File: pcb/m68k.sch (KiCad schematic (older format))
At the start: 14 parts

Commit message: add rtdi sd and ps2
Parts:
- removed U?: IS61C5128AL-10KLI, Package_SO:SOJ-36_10.16x23.49mm_P1.27mm, symbol Memory_RAM:IS61C5128AL-10KLI
- added C?: CP1, symbol Device:CP1
- added C?: 0.1uF, symbol Device:C
- added J?: AudioJack2, symbol Connector:AudioJack2
- added J?: SD_Card, symbol Connector:SD_Card
- added J?: DB15_Male_HighDensity, symbol Connector:DB15_Male_HighDensity
- added J?: USB_B_Micro, symbol Connector:USB_B_Micro
- added J?: Mini-DIN-6, symbol Connector:Mini-DIN-6
- added R? (x2): 120, symbol Device:R
- added R? (x2): 2, symbol Device:R
- added U?: FT232RL, Package_SO:SSOP-28_5.3x10.2mm_P0.65mm, symbol Interface_USB:FT232RL
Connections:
- net labels added: +3.3V, +5V, GND
- wire segments 185 -> 251
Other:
- note removed: "SRAM\n"

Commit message: Cleanup schematic and fix errors
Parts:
- C?: symbol Device:CP1 -> m68k-rescue:CP1-Device
- C?: symbol Device:C -> m68k-rescue:C-Device
- J?: symbol Connector:AudioJack2 -> m68k-rescue:AudioJack2-Connector
- J?: symbol Connector:SD_Card -> m68k-rescue:SD_Card-Connector
- J?: symbol Connector:DB15_Male_HighDensity -> m68k-rescue:DB15_Male_HighDensity-Connector
- J?: symbol Connector:USB_B_Micro -> m68k-rescue:USB_B_Micro-Connector
- J?: symbol Connector:Mini-DIN-6 -> m68k-rescue:Mini-DIN-6-Connector
- R? (x4): symbol Device:R -> m68k-rescue:R-Device
- U?: symbol CPU_NXP_68000:68000D -> m68k-rescue:68000D-CPU_NXP_68000
- U? (x6): symbol Lattice_iCE_FPGA:iCE40-HX4K-TQ144 -> m68k-rescue:iCE40-HX4K-TQ144-Lattice_iCE_FPGA
- U?: symbol Interface_USB:FT232RL -> m68k-rescue:FT232RL-Interface_USB
- U? (x3): symbol Logic_LevelTranslator:TXB0108DQSR -> m68k-rescue:TXB0108DQSR-Logic_LevelTranslator
- U?: symbol Memory_RAM:AS6C1616 -> m68k-rescue:AS6C1616-Memory_RAM
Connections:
- net labels added: a1, a10, a11, a12, a13, a14, a15, a16, a17, a18, a19, a2, a20, a21, a22, a23, a24, a3, a4, a5, a6, a7, a8, a9, d0, d1, d10, d11, d12, d13, d14, d15, d2, d3, d4, d5, d6, d7, d8, d9
- net labels removed: A24, A25, Unnecessary?
- wire segments 251 -> 265
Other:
- note removed: "Could be hooked up directly\n"
- moved on the sheet: U?

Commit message: add vga dac and start control pins
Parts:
- removed R? (x2): 120, symbol m68k-rescue:R-Device
- added C?: 0.1uF, symbol Device:C
- added R?: R, symbol Device:R
- added U?: ADV7125KSTZ50, ST_48, symbol 2019-05-17_15-12-34:ADV7125KSTZ50
- added U? (x2): TXB0108DQSR, Package_SON:USON-20_2x4mm_P0.4mm, symbol m68k-rescue:TXB0108DQSR-Logic_LevelTranslator-m68k-rescue
- C?: symbol m68k-rescue:CP1-Device -> m68k-rescue:CP1-Device-m68k-rescue
- C?: symbol m68k-rescue:C-Device -> m68k-rescue:C-Device-m68k-rescue
- J?: symbol m68k-rescue:AudioJack2-Connector -> m68k-rescue:AudioJack2-Connector-m68k-rescue
- J?: symbol m68k-rescue:SD_Card-Connector -> m68k-rescue:SD_Card-Connector-m68k-rescue
- J?: symbol m68k-rescue:DB15_Male_HighDensity-Connector -> m68k-rescue:DB15_Male_HighDensity-Connector-m68k-rescue
- J?: symbol m68k-rescue:USB_B_Micro-Connector -> m68k-rescue:USB_B_Micro-Connector-m68k-rescue
- J?: symbol m68k-rescue:Mini-DIN-6-Connector -> m68k-rescue:Mini-DIN-6-Connector-m68k-rescue
- R? (x2): symbol m68k-rescue:R-Device -> m68k-rescue:R-Device-m68k-rescue
- U?: symbol m68k-rescue:68000D-CPU_NXP_68000 -> m68k-rescue:68000D-CPU_NXP_68000-m68k-rescue
- U?: symbol m68k-rescue:FT232RL-Interface_USB -> m68k-rescue:FT232RL-Interface_USB-m68k-rescue
- U? (x3): symbol m68k-rescue:TXB0108DQSR-Logic_LevelTranslator -> m68k-rescue:TXB0108DQSR-Logic_LevelTranslator-m68k-rescue
- U?: symbol m68k-rescue:AS6C1616-Memory_RAM -> m68k-rescue:AS6C1616-Memory_RAM-m68k-rescue
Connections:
- net labels added: R0, R1, R2, R3, R4, R5, R6, R7, hsync, vsync
- wire segments 265 -> 437
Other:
- moved on the sheet: R?, U?A, U?C, U?D, U?F

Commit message: Clean-up some signals
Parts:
- added U?: TXB0108DQSR, Package_SON:USON-20_2x4mm_P0.4mm, symbol m68k-rescue:TXB0108DQSR-Logic_LevelTranslator-m68k-rescue
- C?: symbol Device:C -> m68k-rescue:C-Device
- R?: symbol Device:R -> m68k-rescue:R-Device
- U?: symbol 2019-05-17_15-12-34:ADV7125KSTZ50 -> m68k-rescue:ADV7125KSTZ50-2019-05-17_15-12-34
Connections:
- net labels added: ASn, BERRn, BGACKn, BGn, BRn, CLK, DTACKn, E, FC0, FC1, FC2, HALTn, IPL0n, IPL1n, IPL2n, LDSn, RESETn, R_Wn, UDSn, VMAn, VPAn
- wire segments 437 -> 464
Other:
- note added: "Not level converted,\nbut it’ll be fine\n(probably)"
- moved on the sheet: U?, U?A, U?B, U?E, U?F

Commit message: Fix mostly everything
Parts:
- removed C?: CP1, symbol m68k-rescue:CP1-Device-m68k-rescue
- removed C?: 0.1uF, symbol m68k-rescue:C-Device-m68k-rescue
- removed C?: 0.1uF, symbol m68k-rescue:C-Device
- removed J?: AudioJack2, symbol m68k-rescue:AudioJack2-Connector-m68k-rescue
- removed R? (x2): 2, symbol m68k-rescue:R-Device-m68k-rescue
- removed R?: R, symbol m68k-rescue:R-Device
- removed U?: FT232RL, Package_SO:SSOP-28_5.3x10.2mm_P0.65mm, symbol m68k-rescue:FT232RL-Interface_USB-m68k-rescue
- removed U?: TXB0108DQSR, Package_SON:USON-20_2x4mm_P0.4mm, symbol m68k-rescue:TXB0108DQSR-Logic_LevelTranslator-m68k-rescue
- added C1, C10, C11, C12, C13, C14, C15, C16, C17, C18, C19, C2, C21, C22, C4, C6, C7: 0.1uF, symbol Device:C
- added C20: 0.1uF, symbol Device:C_Small
- added C3, C9: 10uF, symbol Device:C
- added C5, C8: 4.7uF, symbol Device:C
- added D1: D_Schottky, symbol Device:D_Schottky
- added D2: AD1580, symbol Device:D
- added R1, R10, R11, R12, R13, R14, R15, R2, R3, R4, R8: 10k, symbol Device:R
- added R16: 1k, symbol Device:R
- added R17, R18, R19: 75, symbol Device:R
- added R20: 530, symbol Device:R_Small
- added R5, R6, R7: 2.2k, symbol Device:R
- added R9: 100, symbol Device:R
- added U1: 93LC56, symbol Memory_EEPROM:93LCxxC
- added U10: 25LCxxx, symbol Memory_EEPROM:25LCxxx
- added U3: FT2232H, symbol Interface_USB:FT2232H
- added X1: ASV-12.000MHz, Oscillator:Oscillator_SMD_Abracon_ASV-4Pin_7.0x5.1mm, symbol Oscillator:ASV-xxxMHz
- gave numbers to parts that had none: 15
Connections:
- net hsync is gone; now on net HSYNC: J4.13
- net vsync is gone; now on net VSYNC: J4.14
- net +3V3: now also J1.1 (VBUS), J3.4 (VDD), U11.5 (VCCA), U11.6 (OE), U12.5 (VCCA), U12.6 (OE), U13.100 (VCCIO_1[2]), U13.123 (VCCIO_0[2]), U13.131 (VCCIO_0[2]), U13.30 (VCCIO_3[2]), U13.46 (VCCIO_2[2]), U13.57 (VCCIO_2[2]), U13.6 (VCCIO_3[2]), U13.72 (VCC_SPI), U13.89 (VCCIO_1[2]), U14.13 (VAA), U14.29 (VAA), U14.30 (VAA), U14.38 (PSAVE*), U4.5 (VCCA), U4.6 (OE), U5.5 (VCCA), U5.6 (OE), U6.5 (VCCA), U6.6 (OE), U7.1 (VCCA), U8.1 (VCCA), U9.37 (VCC), C1.1, C11.1, C12.1, C13.1, C14.1, C15.1, C16.1, C17.1, C19.1, C2.1, C20.2, C21.1, C22.1, C5.1, C6.1, C7.1, C8.1, D1.2 (A), R10.2, R11.2, R12.2, R15.2, R16.2, R2.2, R3.2, R4.2, R6.2, R8.2, U1.6 (ORG), U1.8 (VCC), U10.8 (VCC), U3.20 (VCCIO), U3.31 (VCCIO), U3.4 (VPHY), U3.42 (VCCIO), U3.50 (VREGIN), U3.56 (VCCIO), U3.9 (VPLL), X1.1 (EN), X1.4 (Vdd); no longer J3.3 (VSS), J3.6 (VSS)
- net +5V: now also J4.9, U11.19 (VCCB), U12.19 (VCCB), U2.14 (VCC), U2.49 (VCC), U4.19 (VCCB), U5.19 (VCCB), U6.19 (VCCB), U7.23 (VCCB), U7.24 (VCCB), U8.23 (VCCB), U8.24 (VCCB), R13.1, R14.1; no longer U14.29 (VAA), U14.30 (VAA)
- net ASn: now also U11.16 (B4); no longer U11.17 (B3)
- net BGACKn: now also U13.42 (IOB_64); no longer U12.20 (B1)
- net BGn: now also U11.15 (B5); no longer U12.18 (B2)
- net BRn: now also U13.43 (IOB_71); no longer U12.17 (B3)
- net DTACKn: now also U13.37 (IOB_56); no longer U11.15 (B5)
- net E: now also U11.13 (B7); no longer U12.15 (B5)
- net FC0: now also U12.20 (B1)
- net FC1: now also U12.18 (B2)
- net FC2: now also U12.17 (B3)
- net GND: now also J3.3 (VSS), J3.6 (VSS), J4.10, J4.5, U13.103 (GND[9]), U13.13 (GND[9]), U13.132 (GND[9]), U13.14 (GND[9]), U13.140 (GND[9]), U13.5 (GND[9]), U13.59 (GND[9]), U13.69 (GND[9]), U13.86 (GND[9]), U14.12 (SYNC*), C1.2, C11.2, C12.2, C13.2, C14.2, C15.2, C16.2, C17.2, C18.2, C19.2, C2.2, C21.2, C22.2, C3.2, C4.2, C5.2, C6.2, C7.2, C8.2, D2.2 (A), R1.2, R17.2, R18.2, R19.2, R20.2, R5.2, U1.5 (GND), U10.4 (GND), U3.1 (GND), U3.10 (AGND), U3.11 (GND), U3.13 (TEST), U3.15 (GND), U3.25 (GND), U3.35 (GND), U3.47 (GND), U3.5 (GND), U3.51 (GND), X1.2 (GND); no longer J3.4 (VDD), J4.6, J4.7, J4.8
- net HALTn: now also U11.12 (B8)
- net IPL0n: now also U13.38 (IOB_57); no longer U11.14 (B6)
- net IPL1n: now also U13.39 (IOB_61); no longer U11.13 (B7)
- net IPL2n: now also U13.41 (IOB_63); no longer U11.12 (B8)
- net LDSn: now also U11.17 (B3); no longer U11.18 (B2)
- net RESETn: now also U12.16 (B4), R1.1
- net R_Wn: now also U11.20 (B1); no longer U11.16 (B4)
- net UDSn: now also U11.18 (B2); no longer U11.20 (B1)
- net VMAn: now also U11.14 (B6); no longer U12.16 (B4)
- net VPAn: now also U13.44 (IOB_72); no longer U12.14 (B6)
- net a1: now also U13.134 (IOT_212); no longer U13.130 (IOT_206)
- net a10: now also U13.119 (IOT_178); no longer U13.118 (IOT_177)
- net a11: now also U13.118 (IOT_177); no longer U13.117 (IOT_174)
- net a12: now also U13.117 (IOT_174); no longer U13.116 (IOT_173)
- net a13: now also U13.116 (IOT_173); no longer U13.115 (IOT_172)
- net a14: now also U13.115 (IOT_172); no longer U13.114 (IOT_171)
- net a15: now also U13.114 (IOT_171); no longer U13.113 (IOT_170)
- net a16: now also U13.113 (IOT_170); no longer U13.112 (IOT_169)
- net a17: now also U13.112 (IOT_169); no longer U13.110 (IOT_168)
- net a18: now also U13.110 (IOT_168); no longer U13.30 (VCCIO_3[2]), U13.6 (VCCIO_3[2])
- net a2: now also U13.130 (IOT_206); no longer U13.129 (IOT_198_GBIN0)
- net a3: now also U13.129 (IOT_198_GBIN0); no longer U13.128 (IOT_197_GBIN1)
- net a4: now also U13.128 (IOT_197_GBIN1); no longer U13.125 (IOT_192)
- net a5: now also U13.125 (IOT_192); no longer U13.124 (IOT_191)
- net a6: now also U13.124 (IOT_191); no longer U13.122 (IOT_190)
- net a7: now also U13.122 (IOT_190); no longer U13.121 (IOT_181)
- net a8: now also U13.121 (IOT_181); no longer U13.120 (IOT_179)
- net a9: now also U13.120 (IOT_179); no longer U13.119 (IOT_178)
- net at U11.3 (A3): now also U13.28 (IOL_23A), U9.15 (LB#); no longer U13.134 (IOT_212)
- net at U13.144 (IOT_222): no longer U12.4 (A4)
- net at U13.108 (VPP_2V5): now also D1.1 (K)
- net +1V2: now reaches U13.111 (VCC[4]), U13.27 (VCC[4]), U13.40 (VCC[4]), U13.92 (VCC[4])
- net +1V2: now also R9.2
- net at U13.126 (VCCPLL1): now also U13.54 (VCCPLL0), C10.1, C9.1, R9.1
- net at U13.127 (GNDPLL1): now also U13.53 (GNDPLL0), C10.2, C9.2
- net b6: now reaches U14.22 (B6)
- net b6: now also U13.99 (IOR_152); no longer U13.101 (IOR_160)
- net at U13.102 (IOR_161): now also U14.11 (BLANK*); no longer U14.23 (B7)
- net HSYNC: now reaches U13.105 (IOR_165)
- net VSYNC: now reaches U13.106 (IOR_166)
- net DIR: now reaches U13.107 (IOR_167)
- net DIR: now also U7.2 (DIR), U8.2 (DIR)
- net g0: now reaches U13.82 (IOR_118), U14.3 (G0)
- net g1: now reaches U13.83 (IOR_119), U14.4 (G1)
- net g2: now reaches U13.84 (IOR_120), U14.5 (G2)
- net g3: now reaches U13.85 (IOR_128), U14.6 (G3)
- net g4: now reaches U13.87 (IOR_136), U14.7 (G4)
- net g5: now reaches U13.88 (IOR_137), U14.8 (G5)
- net g6: now reaches U13.90 (IOR_138), U14.9 (G6)
- net g7: now reaches U13.91 (IOR_139), U14.10 (G7)
- net b0: now reaches U13.93 (IOR_140_GBIN3)
- net b0: now also U14.16 (B0); no longer U14.11 (BLANK*)
- net b1: now reaches U13.94 (IOR_141_GBIN2)
- net b1: now also U14.17 (B1); no longer U14.16 (B0)
- net b2: now reaches U13.95 (IOR_144)
- net b2: now also U14.18 (B2); no longer U14.17 (B1)
- net b3: now reaches U13.96 (IOR_146)
- net b3: now also U14.19 (B3); no longer U14.18 (B2)
- net b4: now reaches U13.97 (IOR_147)
- net b4: now also U14.20 (B4); no longer U14.19 (B3)
- net b5: now reaches U13.98 (IOR_148)
- net b5: now also U14.21 (B5); no longer U14.20 (B4)
- net CLK68000: now reaches U13.45 (IOB_73)
- net CLK68000: now also U2.15 (CLK)
- net at U13.47 (IOB_79): now also J3.1 (CD/DAT3)
- net at U13.48 (IOB_80): now also J3.2 (CMD)
- net at U13.49 (IOB_81_GBIN5): now also J3.5 (CLK); no longer J3.2 (CMD)
- net at U13.52 (IOB_82_GBIN4): now also J3.7 (DAT0); no longer J3.5 (CLK)
- net PS2_CLK: now reaches U13.55 (IOB_91)
- net PS2_CLK: now also U12.10 (A8); no longer J3.7 (DAT0)
- net PS2_DATA: now reaches U13.56 (IOB_94)
- net PS2_DATA: now also U12.9 (A7)
- net RX: now reaches U13.61 (IOB_96)
- net RX: now also U3.38 (BDBUS0)
- net TX: now reaches U13.62 (IOB_102)
- net TX: now also U3.39 (BDBUS1)
- net nWP: now reaches U13.63 (IOB_103_CBSEL0)
- net nWP: now also R12.1, U10.3 (~WP)
- net nHOLD: now reaches U13.64 (IOB_104_CBSEL1)
- net nHOLD: now also R11.1, U10.7 (~HOLD)
- net CDONE: now reaches U13.65 (CDONE)
- net CDONE: now also U12.4 (A4), U3.23 (ADBUS6)
- net CRESET_Bn: now reaches U13.66 (CRESET_B)
- net CRESET_Bn: now also R15.1, U3.24 (ADBUS7)
- net at U13.23 (IOL_17A), U9.11 (WE#): now also U11.1 (A1)
- net at U13.26 (IOL_18B), U9.14 (UB#): now also U11.2 (A2); no longer U11.1 (A1)
- net at U13.67 (IOB_105_SDO): now also U10.5 (MOSI), U3.17 (ADBUS1)
- net at U13.68 (IOB_106_SDI): now also U10.2 (MISO), U3.18 (ADBUS2)
- net at U13.70 (IOB_107_SCK): now also R8.1, U10.6 (SCK), U3.16 (ADBUS0)
- net at U13.71 (IOB_108_SS): now also R10.1, U10.1 (~CS), U3.21 (ADBUS4)
- net at J4.1, U14.34 (IOR): now also R17.1
- net at J4.2, U14.32 (IOG): now also R18.1
- net at J4.3, U14.28 (IOB): now also R19.1
- net at J1.3 (D+): now also U3.8 (DP)
- net at J1.2 (D-): now also U3.7 (DM)
- net at U14.35 (COMP): now also C20.1
- net at U14.36 (VREF): now also C18.1, D2.1 (K), R16.1
- net at U14.37 (RSET): now also R20.1
- net at J2.1: now also U12.13 (B7), R14.2
- net at J2.5: now also U12.12 (B8), R13.2
- net CLK renamed clk12
- net clk12: now also U3.2 (OSCI), X1.3 (OUT); no longer U2.15 (CLK)
- net R0 renamed r0
- net R1 renamed r1
- net R2 renamed r2
- net R3 renamed r3
- net R4 renamed r4
- net R5 renamed r5
- net R6 renamed r6
- net R7 renamed r7
- net a24: no longer names the net of U6.10 (A8)
- new net: R6.1, U3.14 (~RESET)
- new net: R5.1, U3.6 (REF)
- new net: R7.1, U1.3 (DI), U3.61 (EEDATA)
- new net: R3.1, U1.2 (SCLK), U3.62 (EECLK)
- new net: R2.1, U1.1 (CS), U3.63 (EECS)
- new net: R4.1, R7.2, U1.4 (DO)
- new net +1V8: C3.1, C4.1, U3.12 (VCORE), U3.37 (VCORE), U3.49 (VREGOUT), U3.64 (VCORE)
- new net b7: U13.101 (IOR_160), U14.23 (B7)
- no-connect marks 0 -> 48
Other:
- note removed: "Not level converted,\nbut it’ll be fine\n(probably)"
- moved on the sheet: J1, J2, J3, J4, U11, U12, U13A, U13B, U13C, U13D, U13E, U13F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

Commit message: Fix VBUS voltage
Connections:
- net +3V3: no longer J1.1 (VBUS)
- net +5V: now also J1.1 (VBUS)
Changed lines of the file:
@@
 	2550 13300 2450 13300
-Wire Wire Line
-	2450 13300 2450 12150
 Wire Wire Line
 	2950 11800 2450 11800
@@
 Wire Wire Line
 	2200 12000 2950 12000
-Wire Wire Line
-	1600 12150 2450 12150
-Connection ~ 2450 12150
-Wire Wire Line
-	2450 12150 2450 11800
 Wire Wire Line
 	1600 12350 2600 12350
@@
 	8050 7700 8050 8000
 Wire Wire Line
-	13800 2500 13850 2550
+	2450 11800 2450 13300
+$Comp
+L power:+5V #PWR?
+U 1 1 733D3E79
+P 1650 11300
+F 0 "#PWR?" H 1650 11150 50  0001 C CNN
+F 1 "+5V" H 1665 11473 50  0000 C CNN
+F 2 "" H 1650 11300 50  0001 C CNN
+F 3 "" H 1650 11300 50  0001 C CNN
+	1    1650 11300
+	1    0    0    -1
+$EndComp
+Wire Wire Line
+	1650 11300 1650 12150
+Wire Wire Line
+	1650 12150 1600 12150
 Wire Bus Line
 	8350 3600 8350 4350
@@
 Wire Bus Line
 	5800 1300 5800 4350
-Connection ~ 13800 2500
-Connection ~ 13850 2550
 $EndSCHEMATC

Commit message: Add various updates and import to Pcbnew
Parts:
- removed R1: 10k, symbol Device:R
- added C23, C30, C31, C32, C33, C34, C35, C37, C38, C39, C41, C44: 0.1uF, Capacitors_SMD:C_0603, symbol Device:C
- added C24, C25, C26, C36, C45: 10uF, Capacitors_SMD:C_0603, symbol Device:C
- added C27, C28, C29: 1uF, Capacitors_SMD:C_0603, symbol Device:C
- added C40, C42, C43: 0.01uF, Capacitors_SMD:C_0603, symbol Device:C
- added R21, R22: 100, Resistors_SMD:R_0603, symbol Device:R
- added R23: 120, Resistors_SMD:R_0603, symbol Device:R
- added U15: 74LVC1G17, TO_SOT_Packages_SMD:SOT-23-5, symbol 74xGxx:74LVC1G17
- added U16: LD1117S33TR_SOT223, TO_SOT_Packages_SMD:SOT-223-3_TabPin2, symbol Regulator_Linear:LD1117S33TR_SOT223
- added U17: LD1117S12TR_SOT223, TO_SOT_Packages_SMD:SOT-223-3_TabPin2, symbol Regulator_Linear:LD1117S12TR_SOT223
- C1, C10, C11, C12, C13, C14, C15, C16, C17, C19, C2, C20, C21, C22, C3, C4, C5, C6, C7, C8, C9: footprint (none) -> Capacitors_SMD:C_0603
- C18: value 0.1uF -> 1uF; footprint (none) -> Capacitors_SMD:C_0603
- D1: footprint (none) -> Diodes_SMD:D_0603
- D2: footprint (none) -> TO_SOT_Packages_SMD:SOT-23
- J1: footprint (none) -> Connectors:USB_Micro-B
- J4: footprint (none) -> Connectors_DSub:DSUB-15-HD_Female_Horizontal_Pitch2.29x1.98mm_EdgePinOffset3.03mm_Housed_MountingHolesOffset4.94mm
- R10, R11, R12, R13, R14, R15, R16, R17, R18, R19, R2, R20, R3, R4, R5, R6, R7, R8, R9: footprint (none) -> Resistors_SMD:R_0603
- U1, U10: footprint (none) -> Housings_SOIC:SOIC-8_3.9x4.9mm_Pitch1.27mm
- U11, U12, U4, U5, U6: footprint Package_SON:USON-20_2x4mm_P0.4mm -> Housings_SON:USON-20_2x4mm_Pitch0.4mm
- U13: footprint (none) -> Housings_QFP:TQFP-144_20x20mm_Pitch0.5mm
- U14: footprint ST_48 -> Housings_QFP:LQFP-48_7x7mm_Pitch0.5mm
- U2: footprint (none) -> Housings_DIP:DIP-64_W15.24mm_Socket_LongPads
- U3: footprint (none) -> Housings_QFP:LQFP-64_10x10mm_Pitch0.5mm
- U7, U8: footprint PW24 -> Housings_SSOP:TSSOP-24_4.4x7.8mm_Pitch0.65mm
- U9: footprint Package_SO:TSOP-I-48_18.4x12mm_P0.5mm -> Housings_SSOP:TSOP-I-48_18.4x12mm_Pitch0.5mm
- X1: footprint Oscillator:Oscillator_SMD_Abracon_ASV-4Pin_7.0x5.1mm -> Oscillators:Oscillator_SMD_Abracon_ASV-4pin_7.0x5.1mm
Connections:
- net BERRn is gone; now on net +5V: U2.22 (BERR)
- net +1V2: now also C25.1, C28.1, C31.1, C34.1, C38.1, C41.1, C43.1, C45.1, R23.1, U17.2 (VO)
- net +3V3: now also U9.12 (CE2), C24.1, C27.1, C30.1, C33.1, C36.1, C37.1, C40.1, C44.1, U16.2 (VO), U17.3 (VI); no longer U4.6 (OE), U5.6 (OE), U6.6 (OE)
- net +5V: now also C23.1, C26.1, C29.1, C32.1, C35.1, C39.1, C42.1, U15.5 (VCC), U16.3 (VI)
- net CLK68000: now also R22.2; no longer U13.45 (IOB_73)
- net GND: now also U9.26 (CE#), C23.2, C24.2, C25.2, C26.2, C27.2, C28.2, C29.2, C30.2, C31.2, C32.2, C33.2, C34.2, C35.2, C36.2, C37.2, C38.2, C39.2, C40.2, C41.2, C42.2, C43.2, C44.2, C45.2, R23.2, U15.3 (GND), U16.1 (GND), U17.1 (GND)
- net clk12: now also R21.1; no longer X1.3 (OUT)
- net ADDR_OE: now reaches U13.144 (IOT_222)
- net ADDR_OE: now also U4.6 (OE), U5.6 (OE), U6.6 (OE)
- net DATA_OEn: now reaches U13.60 (IOB_95)
- net DATA_OEn: now also U7.22 (*OE), U8.22 (*OE)
- net at U13.24 (IOL_17B): no longer U9.26 (CE#)
- net at U13.25 (IOL_18A): no longer U9.12 (CE2)
- new net: U13.45 (IOB_73), U15.2
- new net: R21.2, X1.3 (OUT)
- new net: R22.1, U15.4
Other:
- moved on the sheet: J3

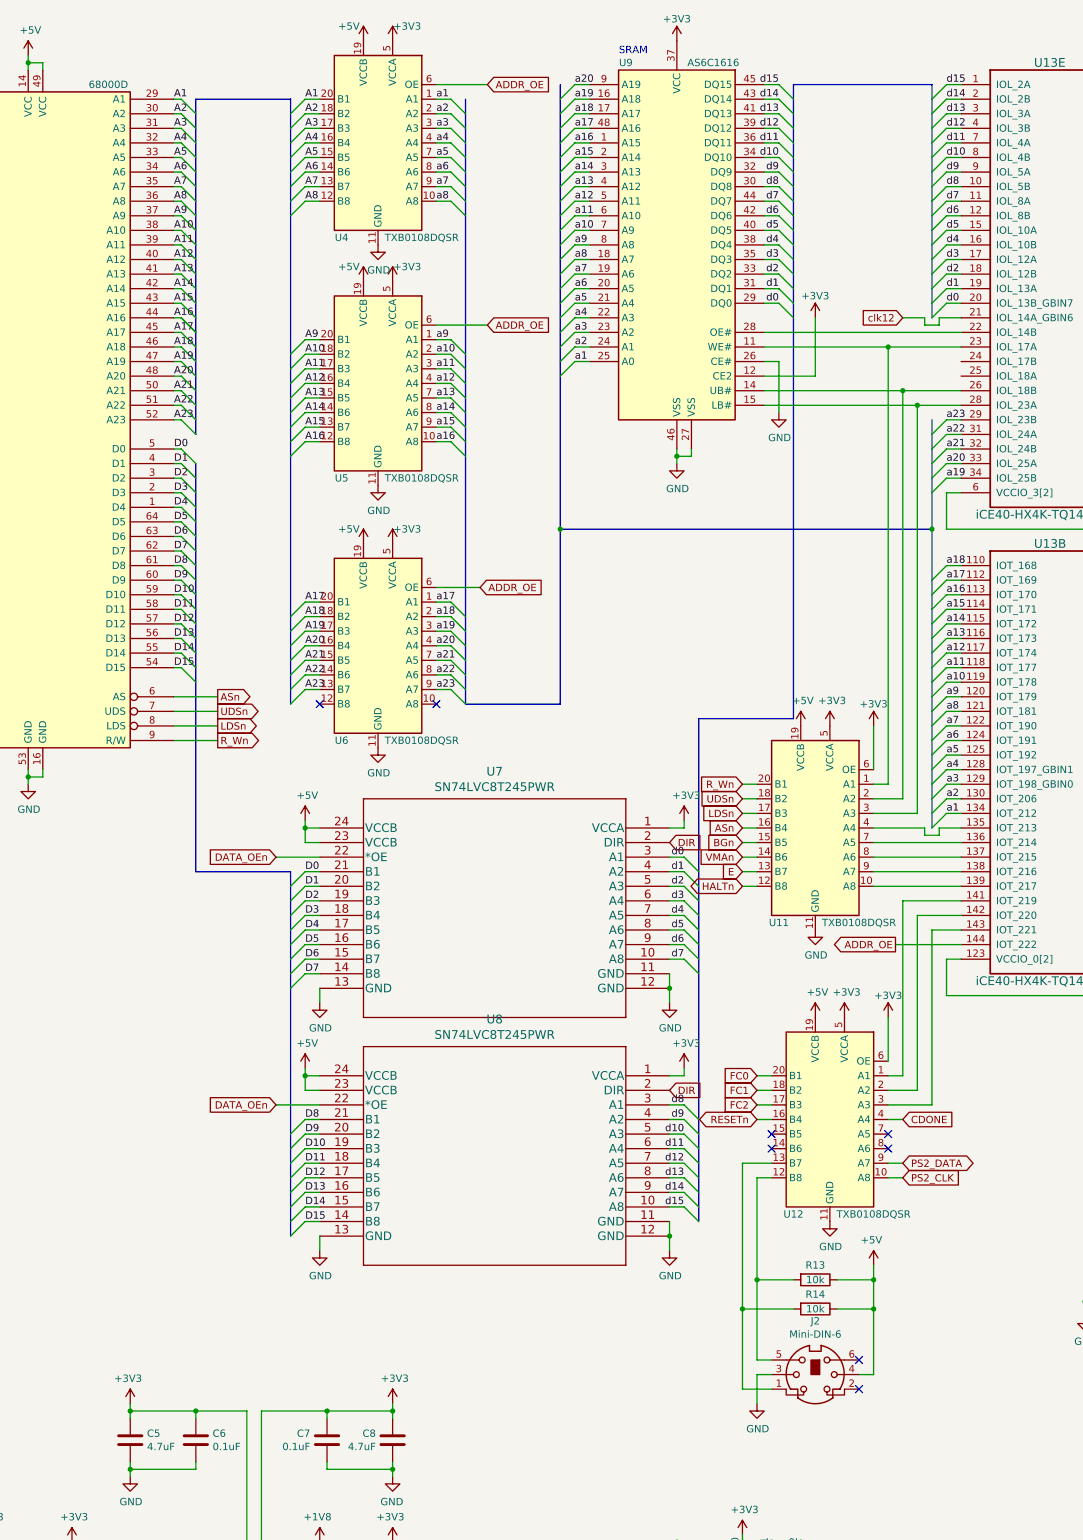
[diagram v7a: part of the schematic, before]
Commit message: Reordered U8 Pins
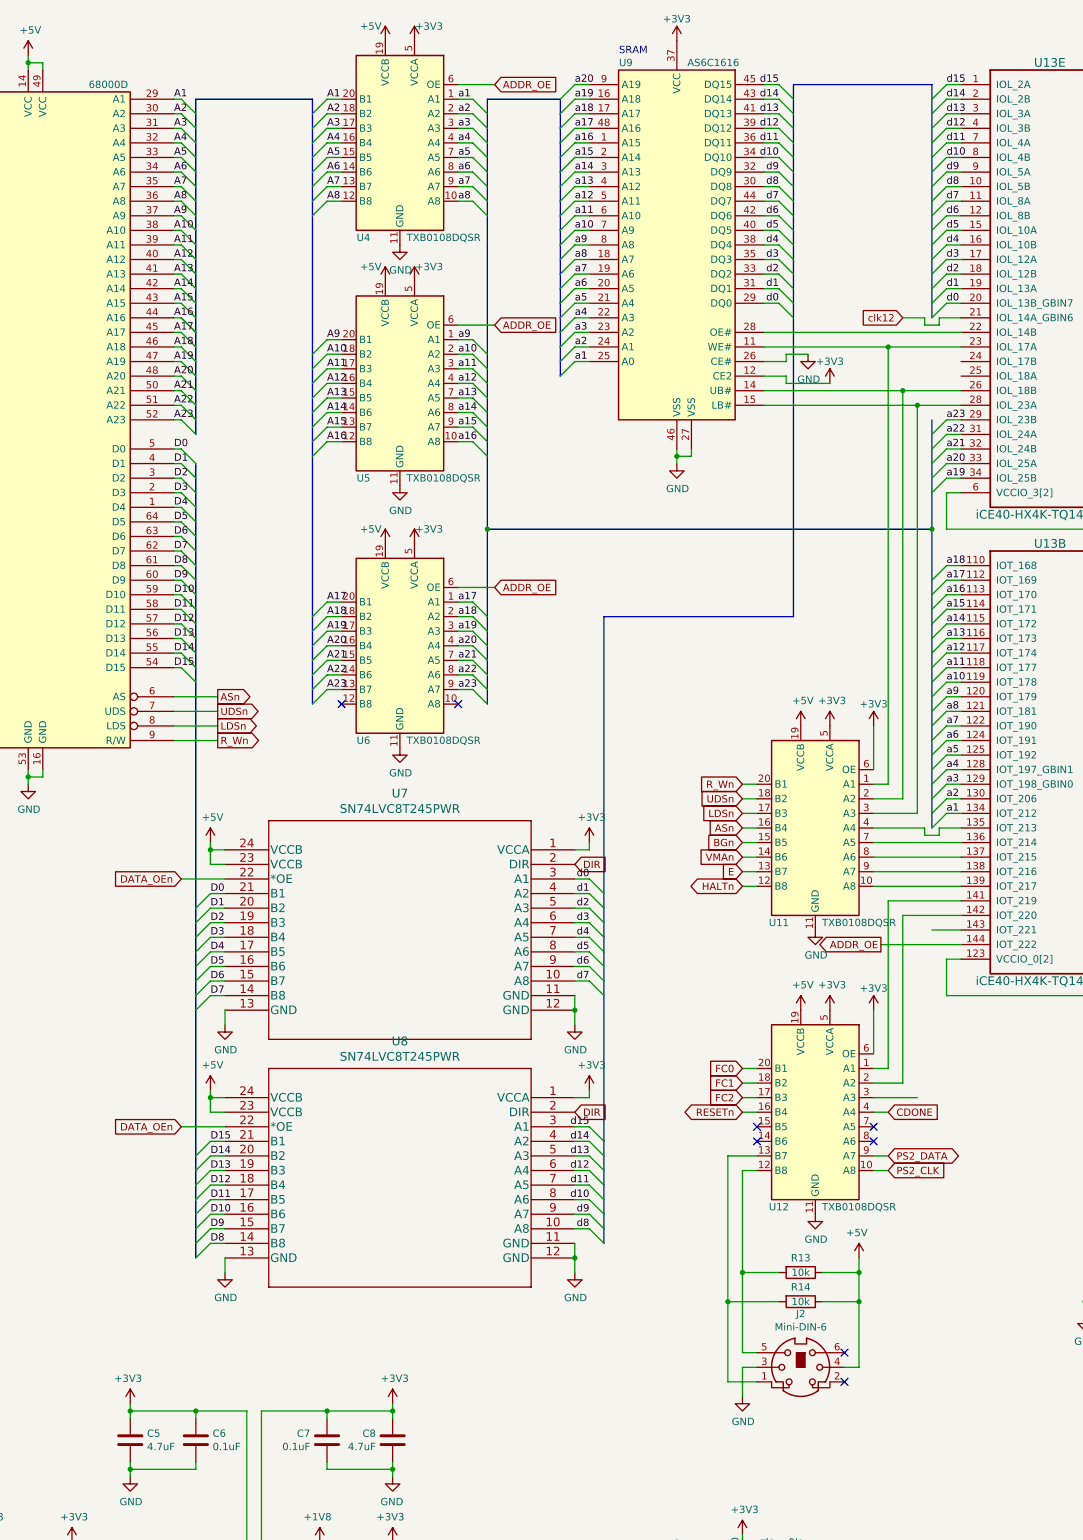
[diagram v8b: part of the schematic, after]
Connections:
- net D10: now also U8.16 (B6); no longer U8.19 (B3)
- net D11: now also U8.17 (B5); no longer U8.18 (B4)
- net D12: now also U8.18 (B4); no longer U8.17 (B5)
- net D13: now also U8.19 (B3); no longer U8.16 (B6)
- net D14: now also U8.20 (B2); no longer U8.15 (B7)
- net D15: now also U8.21 (B1); no longer U8.14 (B8)
- net D8: now also U8.14 (B8); no longer U8.21 (B1)
- net D9: now also U8.15 (B7); no longer U8.20 (B2)
- net d10: now also U8.8 (A6); no longer U8.5 (A3)
- net d11: now also U8.7 (A5); no longer U8.6 (A4)
- net d12: now also U8.6 (A4); no longer U8.7 (A5)
- net d13: now also U8.5 (A3); no longer U8.8 (A6)
- net d14: now also U8.4 (A2); no longer U8.9 (A7)
- net d15: now also U8.3 (A1); no longer U8.10 (A8)
- net d8: now also U8.10 (A8); no longer U8.3 (A1)
- net d9: now also U8.9 (A7); no longer U8.4 (A2)
- net at U13.143 (IOT_221): no longer U12.3 (A3)
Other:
- moved on the sheet: J2, R13, R14, U12, U4, U5, U6, U7, U8
